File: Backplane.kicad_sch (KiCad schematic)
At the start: 11 parts, among them J1 Ext Power in, J2 Int/Ext select, U1 Edge_connector_Male, U2 Edge_connector_Male, U3 Edge_connector_Male, U4 Edge_connector_Male, U5 Edge_connector_Male

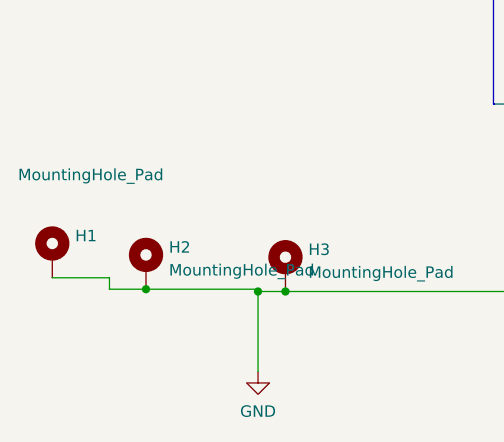
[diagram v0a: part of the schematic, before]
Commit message: Added updated PCB and images. Corrected the fact the sockets were reversed
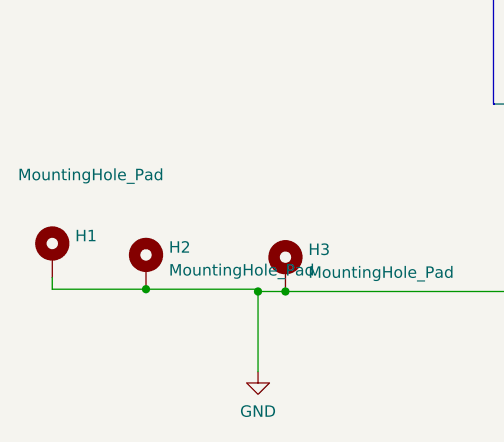
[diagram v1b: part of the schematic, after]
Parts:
- U1: footprint SpeccyEdge:Speccy_edge -> Spectrum:Speccy_edge_External
- U2, U3, U4, U5: footprint SpeccyEdge:Speccy_edge_Socket -> Spectrum:Speccy_edge_Socket_reversed
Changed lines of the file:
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@@
   (junction (at 62.484 24.13) (diameter 0) (color 0 0 0 0)
   )
+  (junction (at 91.44 120.65) (diameter 0) (color 0 0 0 0)
+  )
+  (junction (at 86.36 57.15) (diameter 0) (color 0 0 0 0)
+  )
+  (junction (at 86.36 54.61) (diameter 0) (color 0 0 0 0)
+  )
+  (junction (at 65.786 154.178) (diameter 0) (color 0 0 0 0)
+  )
   (junction (at 50.292 153.924) (diameter 0) (color 0 0 0 0)
   )
-  (junction (at 91.44 120.65) (diameter 0) (color 0 0 0 0)
-  )
-  (junction (at 86.36 57.15) (diameter 0) (color 0 0 0 0)
-  )
-  (junction (at 86.36 54.61) (diameter 0) (color 0 0 0 0)
-  )
-  (junction (at 65.786 154.178) (diameter 0) (color 0 0 0 0)
-  )
   (wire (pts (xy 91.44 96.52) (xy 100.33 96.52))
     (stroke (width 0) (type default) (color 0 0 0 0))
@@
     (stroke (width 0) (type default) (color 0 0 0 0))
   )
-  (wire (pts (xy 39.878 152.654) (xy 46.228 152.654))
-    (stroke (width 0) (type default) (color 0 0 0 0))
-  )
   (wire (pts (xy 91.44 109.22) (xy 100.33 109.22))
     (stroke (width 0) (type default) (color 0 0 0 0))
   )
+  (wire (pts (xy 50.292 153.924) (xy 39.878 153.924))
+    (stroke (width 0) (type default) (color 0 0 0 0))
+  )
   (wire (pts (xy 69.85 29.972) (xy 69.85 24.13))
     (stroke (width 0) (type default) (color 0 0 0 0))
@@
     (stroke (width 0) (type default) (color 0 0 0 0))
   )
+  (wire (pts (xy 39.878 153.924) (xy 39.878 152.654))
+    (stroke (width 0) (type default) (color 0 0 0 0))
+  )
   (bus (pts (xy 184.15 121.92) (xy 135.89 121.92))
     (stroke (width 0) (type default) (color 0 0 0 0))
@@
     (stroke (width 0) (type default) (color 0 0 0 0))
   )
-  (wire (pts (xy 46.228 152.654) (xy 46.228 153.924))
-    (stroke (width 0) (type default) (color 0 0 0 0))
-  )
   (wire (pts (xy 100.33 18.796) (xy 62.992 18.796))
     (stroke (width 0) (type default) (color 0 0 0 0))
@@
   )
   (wire (pts (xy 135.89 83.82) (xy 144.78 83.82))
-    (stroke (width 0) (type default) (color 0 0 0 0))
-  )
-  (wire (pts (xy 46.228 153.924) (xy 50.292 153.924))
     (stroke (width 0) (type default) (color 0 0 0 0))
   )
@@
     (property "Reference" "U2" (id 0) (at 110.49 34.451 0))
     (property "Value" "Edge_connector_Male" (id 1) (at 110.49 36.9879 0))
-    (property "Footprint" "SpeccyEdge:Speccy_edge_Socket" (id 2) (at 72.39 81.28 0)
+    (property "Footprint" "Spectrum:Speccy_edge_Socket_reversed" (id 2) (at 72.39 81.28 0)
       (effects (font (size 1.27 1.27)) hide)
     )
@@
     (property "Reference" "U3" (id 0) (at 154.94 34.451 0))
     (property "Value" "Edge_connector_Male" (id 1) (at 154.94 36.9879 0))
-    (property "Footprint" "SpeccyEdge:Speccy_edge_Socket" (id 2) (at 116.84 81.28 0)
+    (property "Footprint" "Spectrum:Speccy_edge_Socket_reversed" (id 2) (at 116.84 81.28 0)
       (effects (font (size 1.27 1.27)) hide)
     )
@@
     (property "Reference" "U1" (id 0) (at 67.31 35.721 0))
     (property "Value" "Edge_connector_Male" (id 1) (at 67.31 38.2579 0))
-    (property "Footprint" "SpeccyEdge:Speccy_edge" (id 2) (at 29.21 82.55 0)
+    (property "Footprint" "Spectrum:Speccy_edge_External" (id 2) (at 29.21 82.55 0)
       (effects (font (size 1.27 1.27)) hide)
     )
@@
     (property "Reference" "U5" (id 0) (at 248.92 35.721 0))
     (property "Value" "Edge_connector_Male" (id 1) (at 248.92 38.2579 0))
-    (property "Footprint" "SpeccyEdge:Speccy_edge_Socket" (id 2) (at 210.82 82.55 0)
+    (property "Footprint" "Spectrum:Speccy_edge_Socket_reversed" (id 2) (at 210.82 82.55 0)
       (effects (font (size 1.27 1.27)) hide)
     )
@@
     (property "Reference" "U4" (id 0) (at 203.2 35.721 0))
     (property "Value" "Edge_connector_Male" (id 1) (at 203.2 38.2579 0))
-    (property "Footprint" "SpeccyEdge:Speccy_edge_Socket" (id 2) (at 165.1 82.55 0)
+    (property "Footprint" "Spectrum:Speccy_edge_Socket_reversed" (id 2) (at 165.1 82.55 0)
       (effects (font (size 1.27 1.27)) hide)
     )
@@
     )
     (path "/704ba6e6-ee13-4d9d-b544-d836a743bdda"
-      (reference "U1") (unit 1) (value "Edge_connector_Male") (footprint "SpeccyEdge:Speccy_edge")
+      (reference "U1") (unit 1) (value "Edge_connector_Male") (footprint "Spectrum:Speccy_edge_External")
     )
     (path "/003fc4b1-398c-4b09-8e93-cef9b84d6643"
-      (reference "U2") (unit 1) (value "Edge_connector_Male") (footprint "SpeccyEdge:Speccy_edge_Socket")
+      (reference "U2") (unit 1) (value "Edge_connector_Male") (footprint "Spectrum:Speccy_edge_Socket_reversed")
     )
     (path "/385b4e1c-6faa-4661-81f6-ee8c29591e09"
-      (reference "U3") (unit 1) (value "Edge_connector_Male") (footprint "SpeccyEdge:Speccy_edge_Socket")
+      (reference "U3") (unit 1) (value "Edge_connector_Male") (footprint "Spectrum:Speccy_edge_Socket_reversed")
     )
     (path "/aa225a7e-1d48-40b5-93fa-6602a111bee1"
-      (reference "U4") (unit 1) (value "Edge_connector_Male") (footprint "SpeccyEdge:Speccy_edge_Socket")
+      (reference "U4") (unit 1) (value "Edge_connector_Male") (footprint "Spectrum:Speccy_edge_Socket_reversed")
     )
     (path "/81570871-6751-4ca3-b882-77df9d1e2cf0"
-      (reference "U5") (unit 1) (value "Edge_connector_Male") (footprint "SpeccyEdge:Speccy_edge_Socket")
-    )
-  )
+      (reference "U5") (unit 1) (value "Edge_connector_Male") (footprint "Spectrum:Speccy_edge_Socket_reversed")
+    )
+  )
